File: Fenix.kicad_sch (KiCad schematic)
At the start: 4 parts

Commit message: Completed parts library
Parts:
- added U5: (no value), Parts:Adafruit_GPSFeather, symbol Parts:Adafruit_GPSWing
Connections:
- net +3V3: now also U1.2 (3vo), U2.5 (VCC), U2.8 (VCC), U5.2 (3V3); no longer U1. (ADR), U2. (V+)
- net +5V: now also U2.6 (V+), U2.7 (V+); no longer U2. (V+)
- net GND: now also U1.3 (GND), U2.1 (GND), U2.12 (GND), U5.4 (GND); no longer U1. (ADR), U2. (V+)
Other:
- note added: "GPS & Real-Time Clock Module"

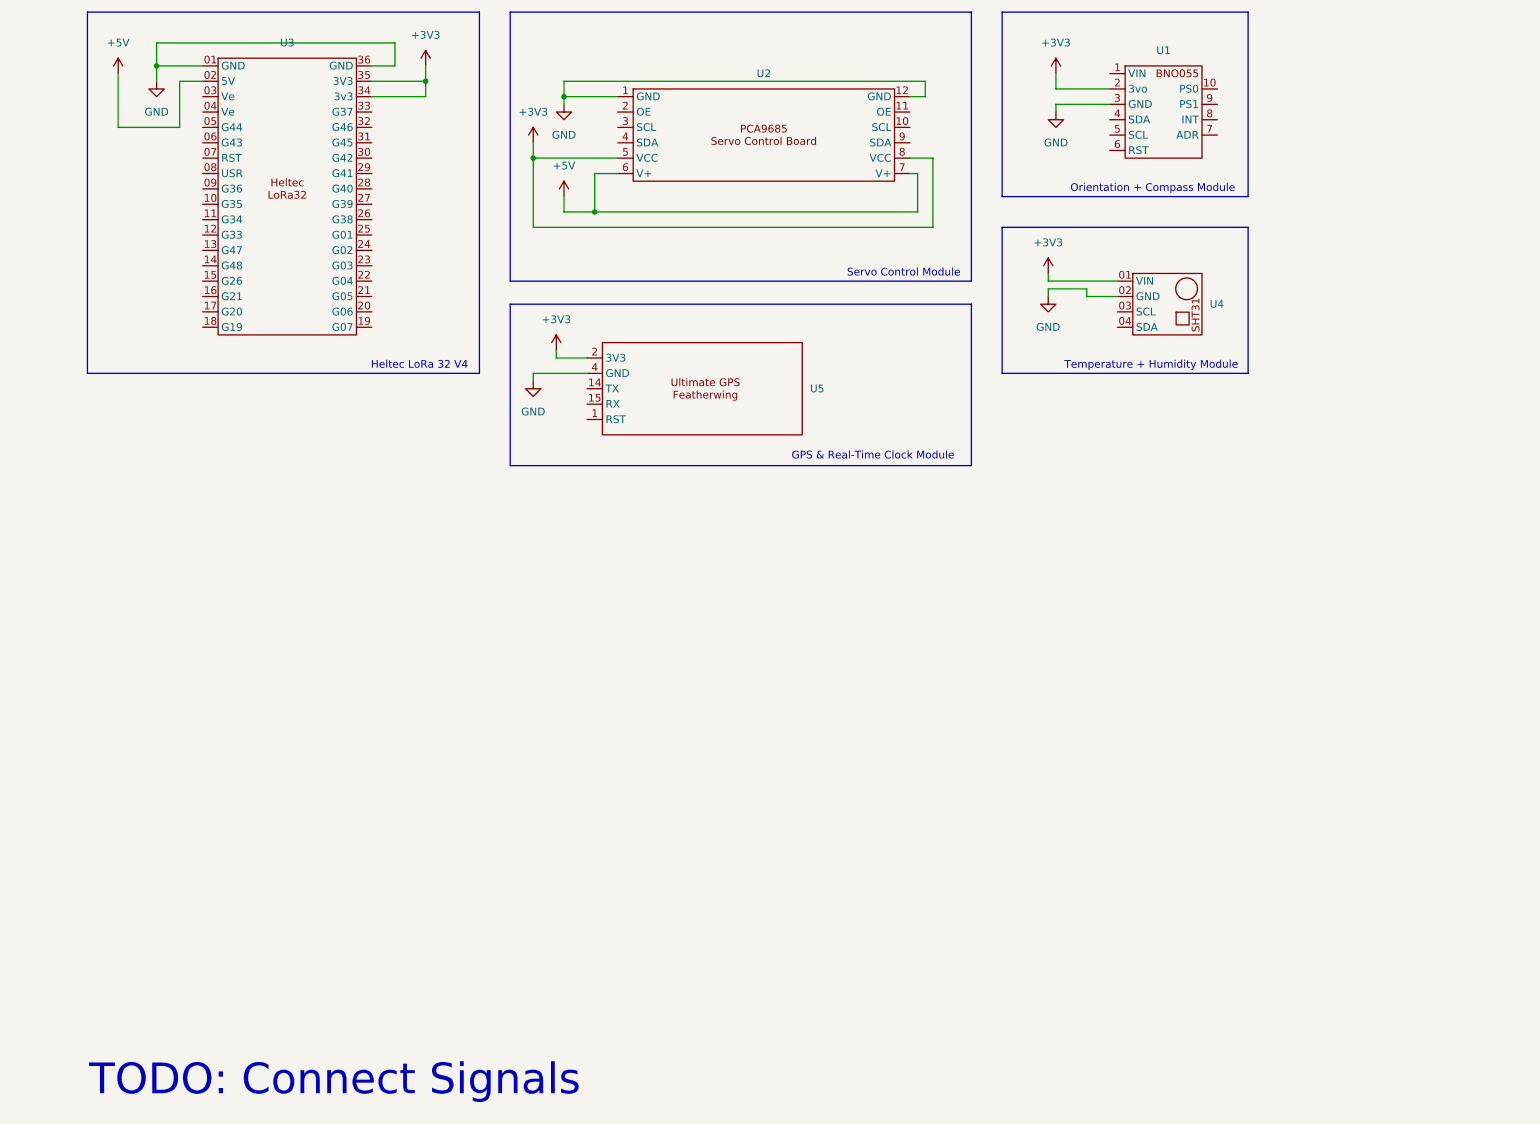
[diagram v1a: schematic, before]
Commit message: Added ToDos in schematic
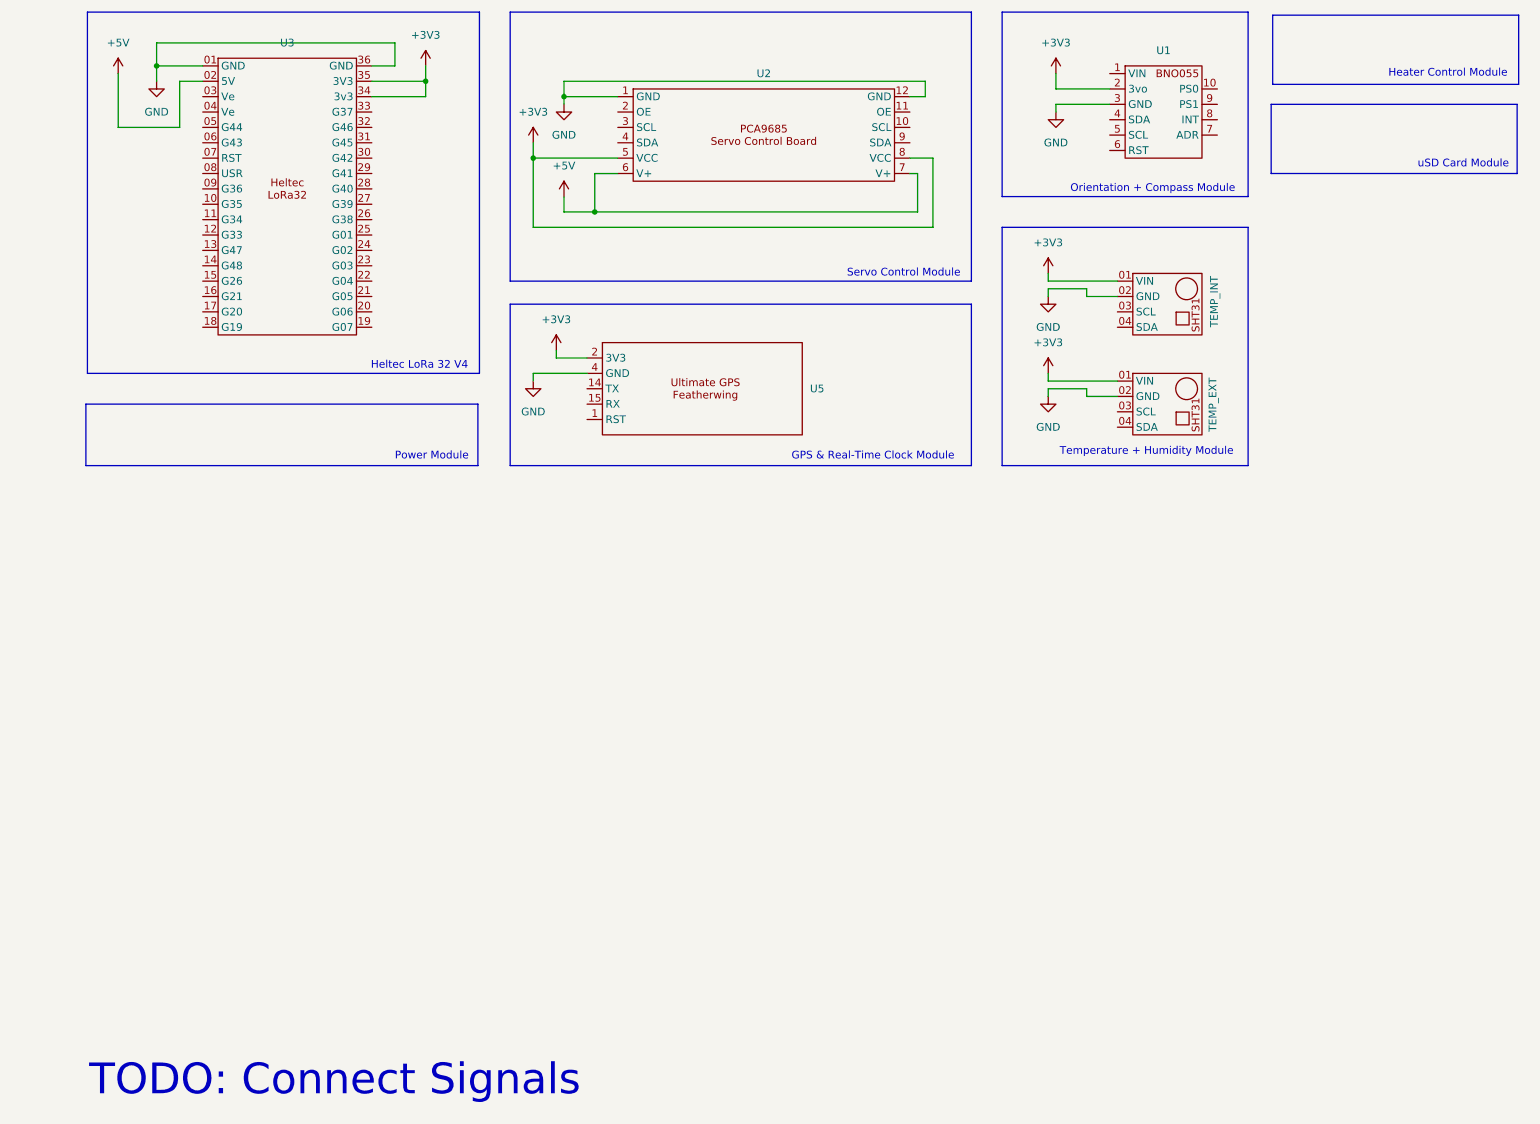
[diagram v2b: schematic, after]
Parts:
- added TEMP_EXT: (no value), Parts:GY-SHT31-D, symbol Parts:GY-SHT31-D
- renumbered U4 to TEMP_INT
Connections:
- net +3V3: now also TEMP_EXT.01 (VIN)
- net GND: now also TEMP_EXT.02 (GND)
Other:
- note added: "Heater Control Module"
- note added: "Power Module"
- note added: "uSD Card Module"

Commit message: Added uSD + Power connector
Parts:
- added J1: PWR, TerminalBlock:TerminalBlock_MaiXu_MX126-5.0-02P_1x02_P5.00mm, symbol Connector:Screw_Terminal_01x02
- added J2: RELAY_CTRL, TerminalBlock:TerminalBlock_MaiXu_MX126-5.0-02P_1x02_P5.00mm, symbol Connector:Screw_Terminal_01x02
- added U4: (no value), Parts:Generic_uSD, symbol Parts:Generic_uSD
- renumbered TEMP_EXT to TEMP_EXT1, TEMP_INT to TEMP_INT1
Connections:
- net +3V3: now also U4.1 (3V3)
- net GND: now also U4.6 (GND)
- net I2C_CLK: now reaches TEMP_INT1.03 (SCL)
- net I2C_CLK: now also TEMP_EXT1.03 (SCL)
- net I2C_DATA: now reaches TEMP_INT1.04 (SDA)
- net I2C_DATA: now also TEMP_EXT1.04 (SDA)
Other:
- moved on the sheet: TEMP_EXT1, TEMP_INT1, U5
